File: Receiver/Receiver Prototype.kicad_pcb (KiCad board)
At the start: 4 copper layers, 145 x 50.8 mm, 108 parts, among them J1 Conn_01x02_Socket, J10 Conn_01x01, J11 Conn_Coaxial, J12 Conn_Coaxial, J13 Conn_Coaxial, J14 Conn_Coaxial, J15 Conn_01x01, J16 Conn_01x01, J17 Conn_01x02, J18 Conn_01x02, J19 Conn_01x01, J2 Conn_01x01, J20 Conn_01x01, J21 Conn_01x01, J22 Conn_01x01, J23 Conn_01x02, J24 Conn_01x02, J25 Conn_01x01, J26 Conn_01x03, J27 Conn_01x03, J28 Conn_01x02, J29 Conn_01x03, J3 Conn_01x01, J30 Conn_01x03, J4 Conn_Coaxial, J5 Conn_01x01, J6 Conn_01x02, J7 Conn_Coaxial, J8 Conn_Coaxial, J9 Conn_01x01, U1 OPA3692ID, U2 AD8692ARZ, U3 OPA692IDBVR, U4 LT3045EMSE-PBF, U5 AD607ARSZ, U6 LT3094EMSE-PBF

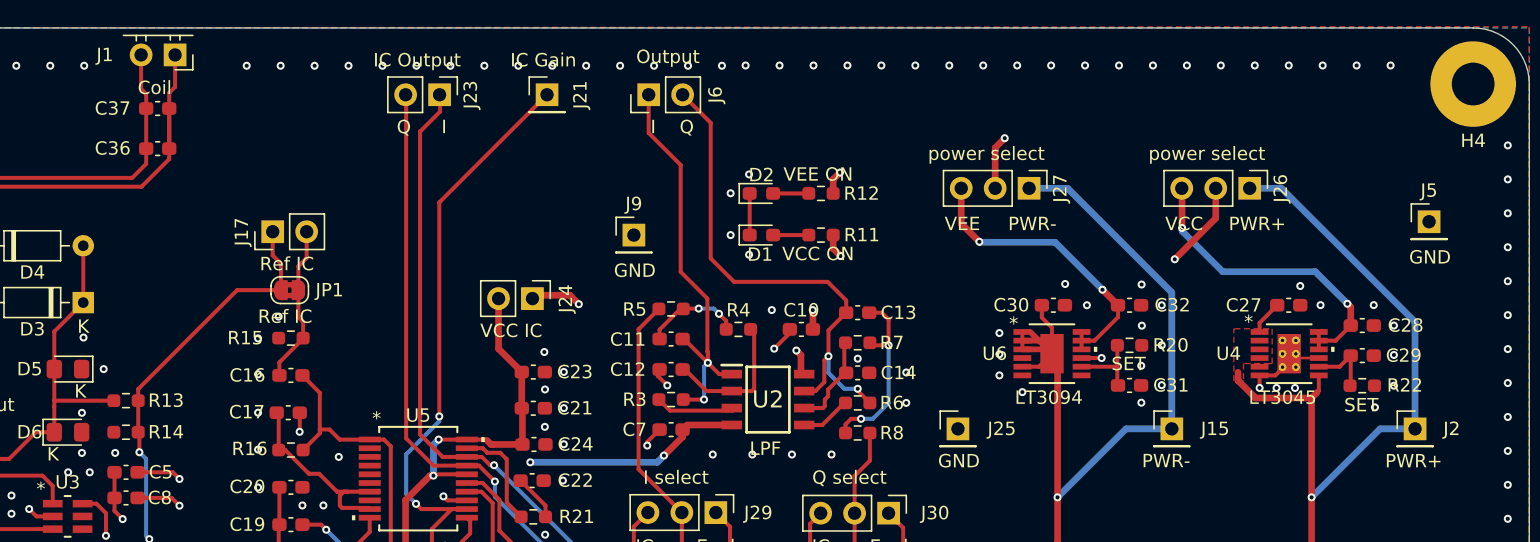
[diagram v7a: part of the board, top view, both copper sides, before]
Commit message: Connected COM1 to Ground in AD607
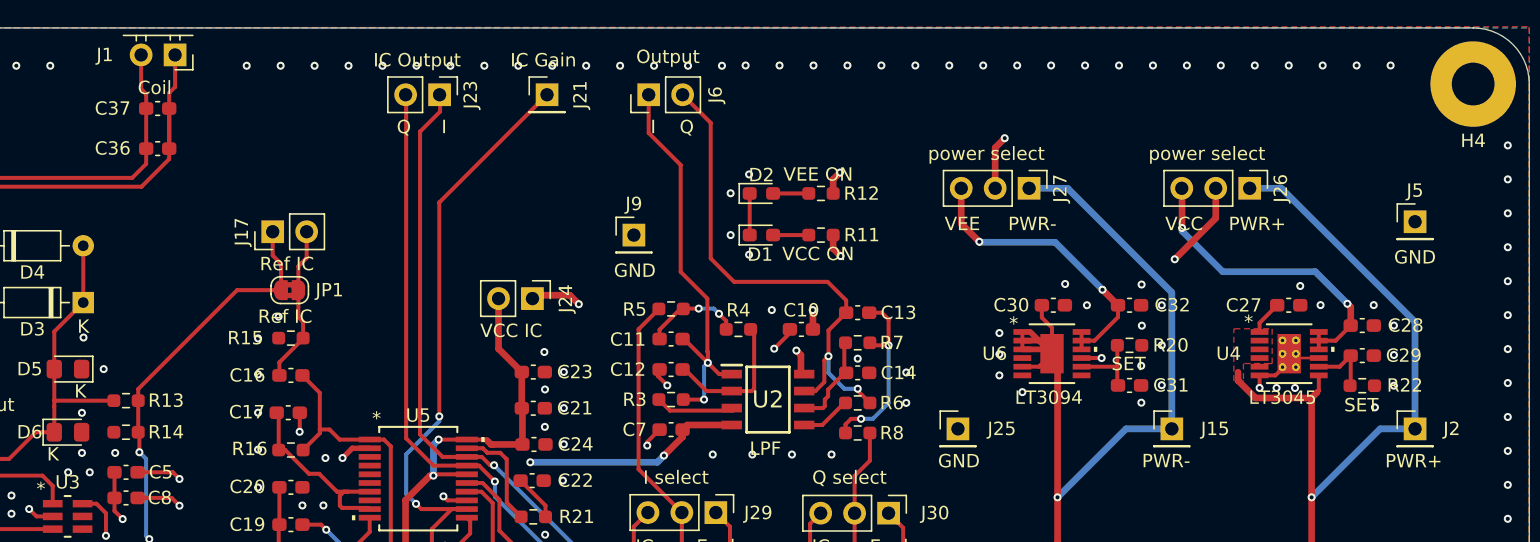
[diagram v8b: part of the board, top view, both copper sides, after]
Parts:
- moved J5 1.05 mm to (223.2, 64.5)
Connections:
- U5 pad 2: unconnected-(U5-COM1-Pad2) -> GND
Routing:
- net GND: track 25.1 -> 27.4 mm
